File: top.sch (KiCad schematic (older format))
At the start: 0 parts

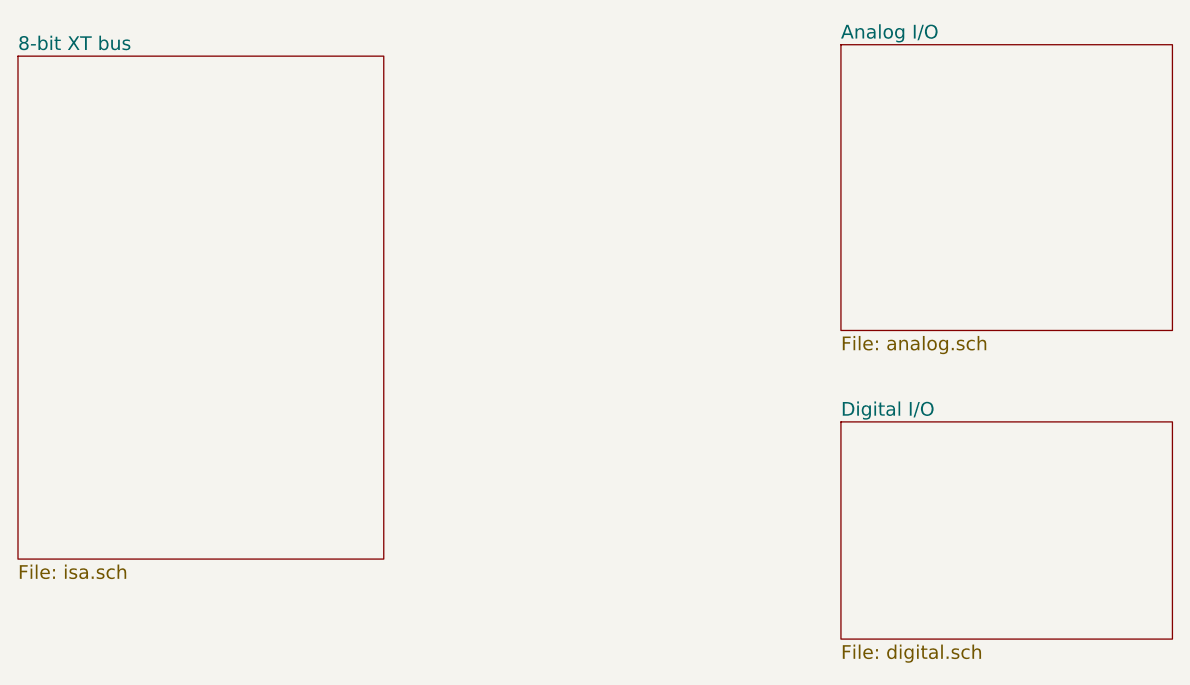
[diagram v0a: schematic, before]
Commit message: Fixed schematic to work with KiCad 5
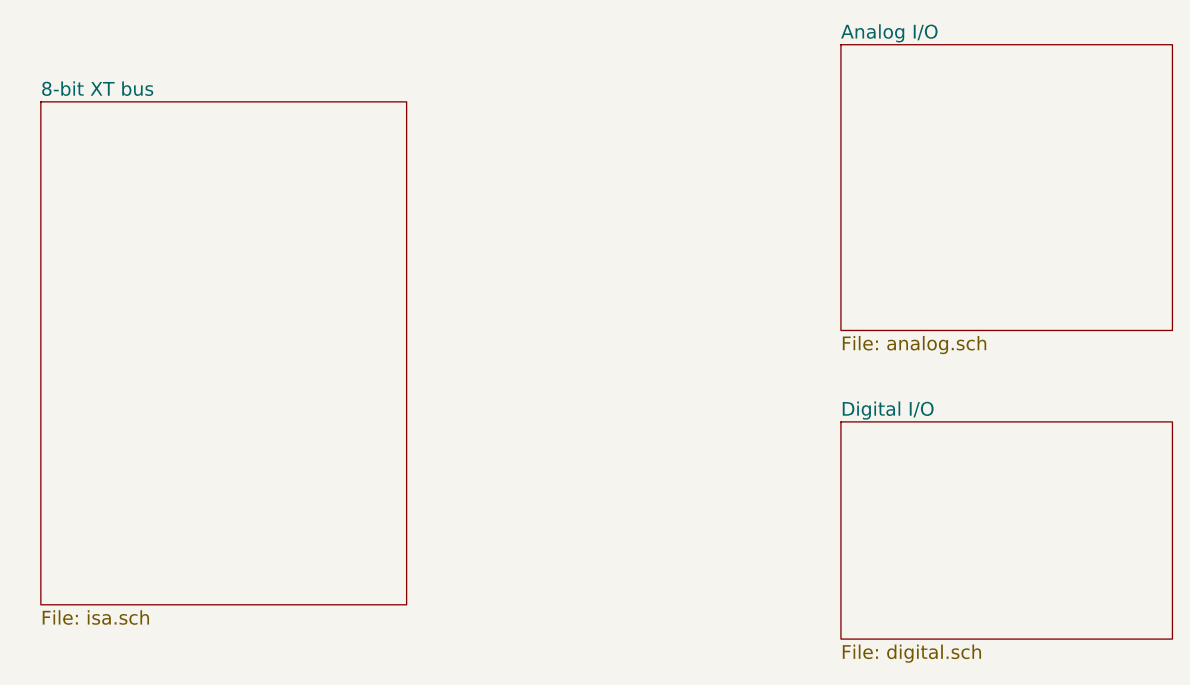
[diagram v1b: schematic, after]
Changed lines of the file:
@@
-EESchema Schematic File Version 2
-LIBS:power
-LIBS:device
-LIBS:switches
-LIBS:relays
-LIBS:motors
-LIBS:transistors
-LIBS:conn
-LIBS:linear
-LIBS:regul
-LIBS:74xx
-LIBS:cmos4000
-LIBS:adc-dac
-LIBS:memory
-LIBS:xilinx
-LIBS:microcontrollers
-LIBS:dsp
-LIBS:microchip
-LIBS:analog_switches
-LIBS:motorola
-LIBS:texas
-LIBS:intel
-LIBS:audio
-LIBS:interface
-LIBS:digital-audio
-LIBS:philips
-LIBS:display
-LIBS:cypress
-LIBS:siliconi
-LIBS:opto
-LIBS:atmel
-LIBS:contrib
-LIBS:valves
-EELAYER 25 0
+EESchema Schematic File Version 4
+EELAYER 26 0
 EELAYER END
 $Descr A4 11693 8268
 encoding utf-8
-Sheet 1 3
+Sheet 1 5
 Title ""
 Date ""
@@
 $EndDescr
 $Sheet
-S 2150 2150 1600 2200
+S 2250 2350 1600 2200
 U 5B426208
 F0 "8-bit XT bus" 60
